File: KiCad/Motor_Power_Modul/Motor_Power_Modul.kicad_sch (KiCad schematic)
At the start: 22 parts, among them J1 Power Input, J2 Power Out, J3 Power Out, J4 Motor Output, J5 Input, J6 Dead Man, Q1 IRF3708, Q2 IRF3708, U1 IR2302

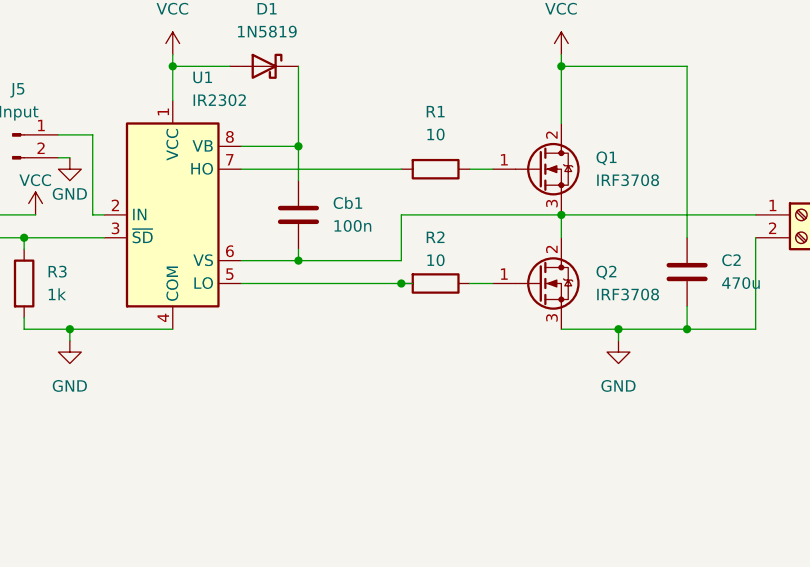
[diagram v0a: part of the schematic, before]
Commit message: Iteration 2 von DC/DC Wandler
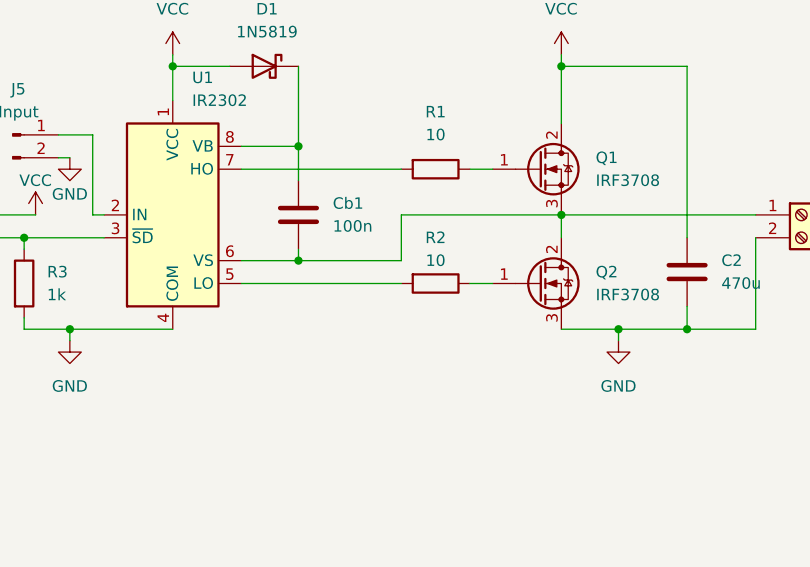
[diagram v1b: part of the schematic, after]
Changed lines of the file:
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@@
-	)
-	(junction
-		(at 116.84 45.72)
-		(diameter 0)
-		(color 0 0 0 0)
 	)
 	(junction
@@
 	(wire
 		(pts
-			(xy 118.11 45.72) (xy 116.84 45.72)
-		)
-		(stroke
-			(width 0)
-			(type default)
-		)
-	)
-	(wire
-		(pts
 			(xy 74.93 50.8) (xy 80.01 50.8)
 		)
@@
 	(wire
 		(pts
+			(xy 44.45 21.59) (xy 44.45 35.56)
+		)
+		(stroke
+			(width 0)
+			(type default)
+		)
+	)
+	(wire
+		(pts
+			(xy 91.44 21.59) (xy 91.44 25.4)
+		)
+		(stroke
+			(width 0)
+			(type default)
+		)
+	)
+	(wire
+		(pts
+			(xy 74.93 49.53) (xy 74.93 50.8)
+		)
+		(stroke
+			(width 0)
+			(type default)
+		)
+	)
+	(wire
+		(pts
+			(xy 45.72 52.07) (xy 45.72 50.8)
+		)
+		(stroke
+			(width 0)
+			(type default)
+		)
+	)
+	(wire
+		(pts
+			(xy 45.72 38.1) (xy 45.72 50.8)
+		)
+		(stroke
+			(width 0)
+			(type default)
+		)
+	)
+	(wire
+		(pts
+			(xy 91.44 20.32) (xy 91.44 21.59)
+		)
+		(stroke
+			(width 0)
+			(type default)
+		)
+	)
+	(wire
+		(pts
+			(xy 50.8 50.8) (xy 45.72 50.8)
+		)
+		(stroke
+			(width 0)
+			(type default)
+		)
+	)
+	(wire
+		(pts
+			(xy 82.55 29.21) (xy 82.55 38.1)
+		)
+		(stroke
+			(width 0)
+			(type default)
+		)
+	)
+	(wire
+		(pts
+			(xy 99.06 33.02) (xy 116.84 33.02)
+		)
+		(stroke
+			(width 0)
+			(type default)
+		)
+	)
+	(wire
+		(pts
+			(xy 99.06 43.18) (xy 105.41 43.18)
+		)
+		(stroke
+			(width 0)
+			(type default)
+		)
+	)
+	(wire
+		(pts
 			(xy 99.06 45.72) (xy 116.84 45.72)
 		)
 		(stroke
-			(width 0)
-			(type default)
-		)
-	)
-	(wire
-		(pts
-			(xy 44.45 21.59) (xy 44.45 35.56)
-		)
-		(stroke
-			(width 0)
-			(type default)
-		)
-	)
-	(wire
-		(pts
-			(xy 91.44 21.59) (xy 91.44 25.4)
-		)
-		(stroke
-			(width 0)
-			(type default)
-		)
-	)
-	(wire
-		(pts
-			(xy 74.93 49.53) (xy 74.93 50.8)
-		)
-		(stroke
-			(width 0)
-			(type default)
-		)
-	)
-	(wire
-		(pts
-			(xy 45.72 52.07) (xy 45.72 50.8)
-		)
-		(stroke
-			(width 0)
-			(type default)
-		)
-	)
-	(wire
-		(pts
-			(xy 45.72 38.1) (xy 45.72 50.8)
-		)
-		(stroke
-			(width 0)
-			(type default)
-		)
-	)
-	(wire
-		(pts
-			(xy 91.44 20.32) (xy 91.44 21.59)
-		)
-		(stroke
-			(width 0)
-			(type default)
-		)
-	)
-	(wire
-		(pts
-			(xy 50.8 50.8) (xy 45.72 50.8)
-		)
-		(stroke
-			(width 0)
-			(type default)
-		)
-	)
-	(wire
-		(pts
-			(xy 82.55 29.21) (xy 82.55 38.1)
-		)
-		(stroke
-			(width 0)
-			(type default)
-		)
-	)
-	(wire
-		(pts
-			(xy 99.06 33.02) (xy 116.84 33.02)
-		)
-		(stroke
-			(width 0)
-			(type default)
-		)
-	)
-	(wire
-		(pts
-			(xy 99.06 43.18) (xy 105.41 43.18)
-		)
-		(stroke
